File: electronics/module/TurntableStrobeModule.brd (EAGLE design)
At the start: 25.1 x 20.3 mm, 11 parts, among them IC1 TINY25, J1 ISP, Q1 12MHz

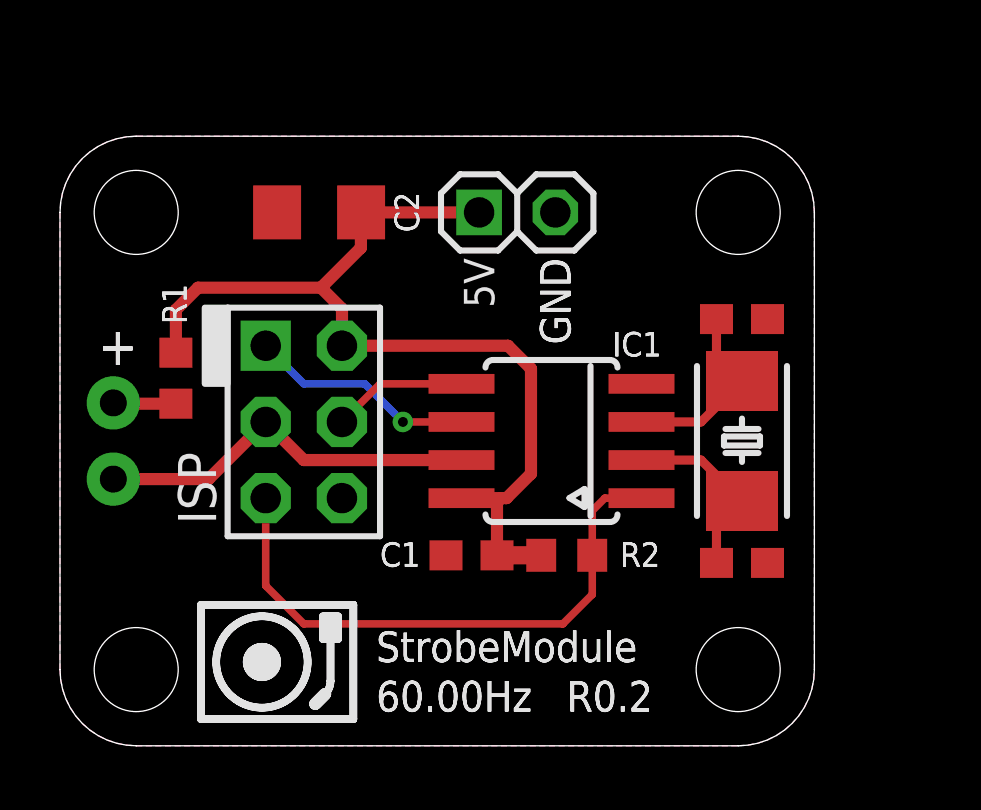
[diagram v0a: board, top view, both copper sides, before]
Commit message: added regulator onboard, changed some packages
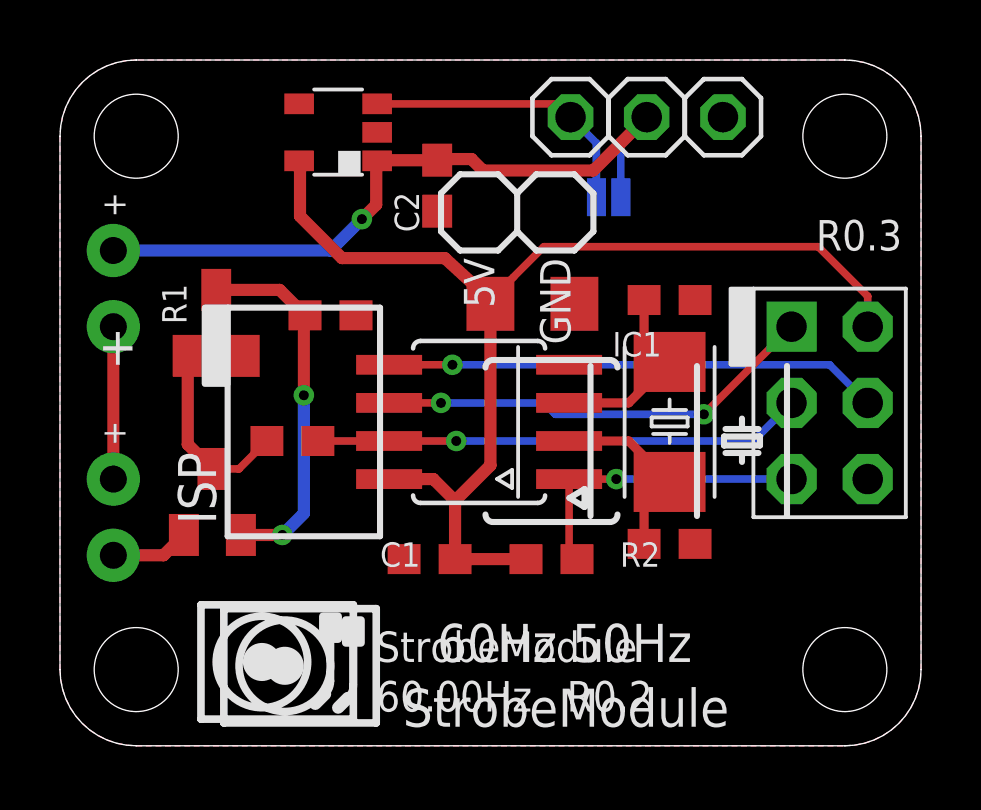
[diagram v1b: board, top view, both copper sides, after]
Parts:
- added C3: 0.1uF, bt_rcl:0603
- added IC2: LP2980M5, bt_regulator:SOT23-5
- added JP2: VIN, bt_electromech:1X01-S
- added JP3: GND, bt_electromech:1X01-S
- added JP4: EN-VIN, SparkFun-Jumpers:SMT-JUMPER_2_NO_SILK
- added LED2: (no value), bt_opto:LED5MMRA
- added Q2, Q3: 2222, bt_transistor:SOT-23
- added R3: 39, bt_rcl:0603
- added U$6: BTLOGO-LOGO-MD, bt:BTLOGOM
- C1, C4, C5: device rcl:C0603 -> bt_rcl:0603
- C2: device rcl:C1206 -> bt_rcl:1206
- JP1: value 5V -> EN; device pinhead-2:1X02-S -> bt_electromech:1X01-S
- Q1: value 12MHz -> (none)
- R1: value 330 -> 10k; device rcl:R0603 -> bt_rcl:0603
- R2: device rcl:R0603 -> bt_rcl:0603
- moved J1 17.5 mm to (25.7, 11.4)
- moved C2 7.74 mm to (15.7, 14.7), turned to 0 degrees
- moved LED1 5.08 mm to (1.78, 15.2)
- moved R1 4.41 mm to (7.75, 10.2), turned to 0 degrees
- moved JP1 3.64 mm to (17.0, 21.0), turned to 270 degrees
- moved C4 2.50 mm to (20.3, 6.73)
- moved C5 2.50 mm to (20.3, 14.9)
- moved Q1 2.50 mm to (20.3, 10.8)
- moved IC1 2.50 mm to (14.0, 10.8)
- moved C1 1.40 mm to (12.3, 6.22)
- moved R2 0.52 mm to (16.4, 6.22)
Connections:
- new net 9V: C3.1, IC2.1, JP2.1, JP4.2, LED1.A
- new net N$1: Q2.3, Q3.1, R1.1
- new net N$2: LED1.C, LED2.A
- new net N$4: Q2.2, Q3.3, R3.2
- new net N$5: IC2.3, JP1.1, JP4.1
- net GND: now also C3.2, IC2.2, JP3.1, Q3.2, R3.1; no longer JP1.2
- net N$3: now also LED2.C, Q2.1; no longer LED1.A, R1.2
- net PB2: now also R1.2; no longer LED1.C
- net VCC: now also IC2.5; no longer JP1.1, R1.1
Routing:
- net 9V: track 0.00 -> 23.8 mm, vias 0 -> 1
- net N$4: track 0.00 -> 12.3 mm, vias 0 -> 2
- net PB0: track 4.51 -> 16.5 mm, vias 0 -> 1
- net N$5: track 0.00 -> 9.65 mm
- net PB5: track 19.3 -> 10.2 mm, vias 0 -> 1
- net PB1: track 7.58 -> 14.8 mm, vias 1 -> 2
- net VCC: track 32.0 -> 38.3 mm
- net N$1: track 0.00 -> 6.31 mm
- net N$2: track 0.00 -> 5.08 mm
- net PB2: track 12.9 -> 16.3 mm, vias 0 -> 1
- net N$3: track 2.10 -> 2.63 mm
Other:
- board size 25.1 x 20.3 mm -> 28.7 x 22.9 mm
- board text added: "60Hz 50Hz"
- board text added: "R0.3"
- board text added: "VIN: 5.5-12V"
- board text added: "cc-by-sa"
